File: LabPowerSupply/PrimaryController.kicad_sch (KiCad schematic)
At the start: 19 parts

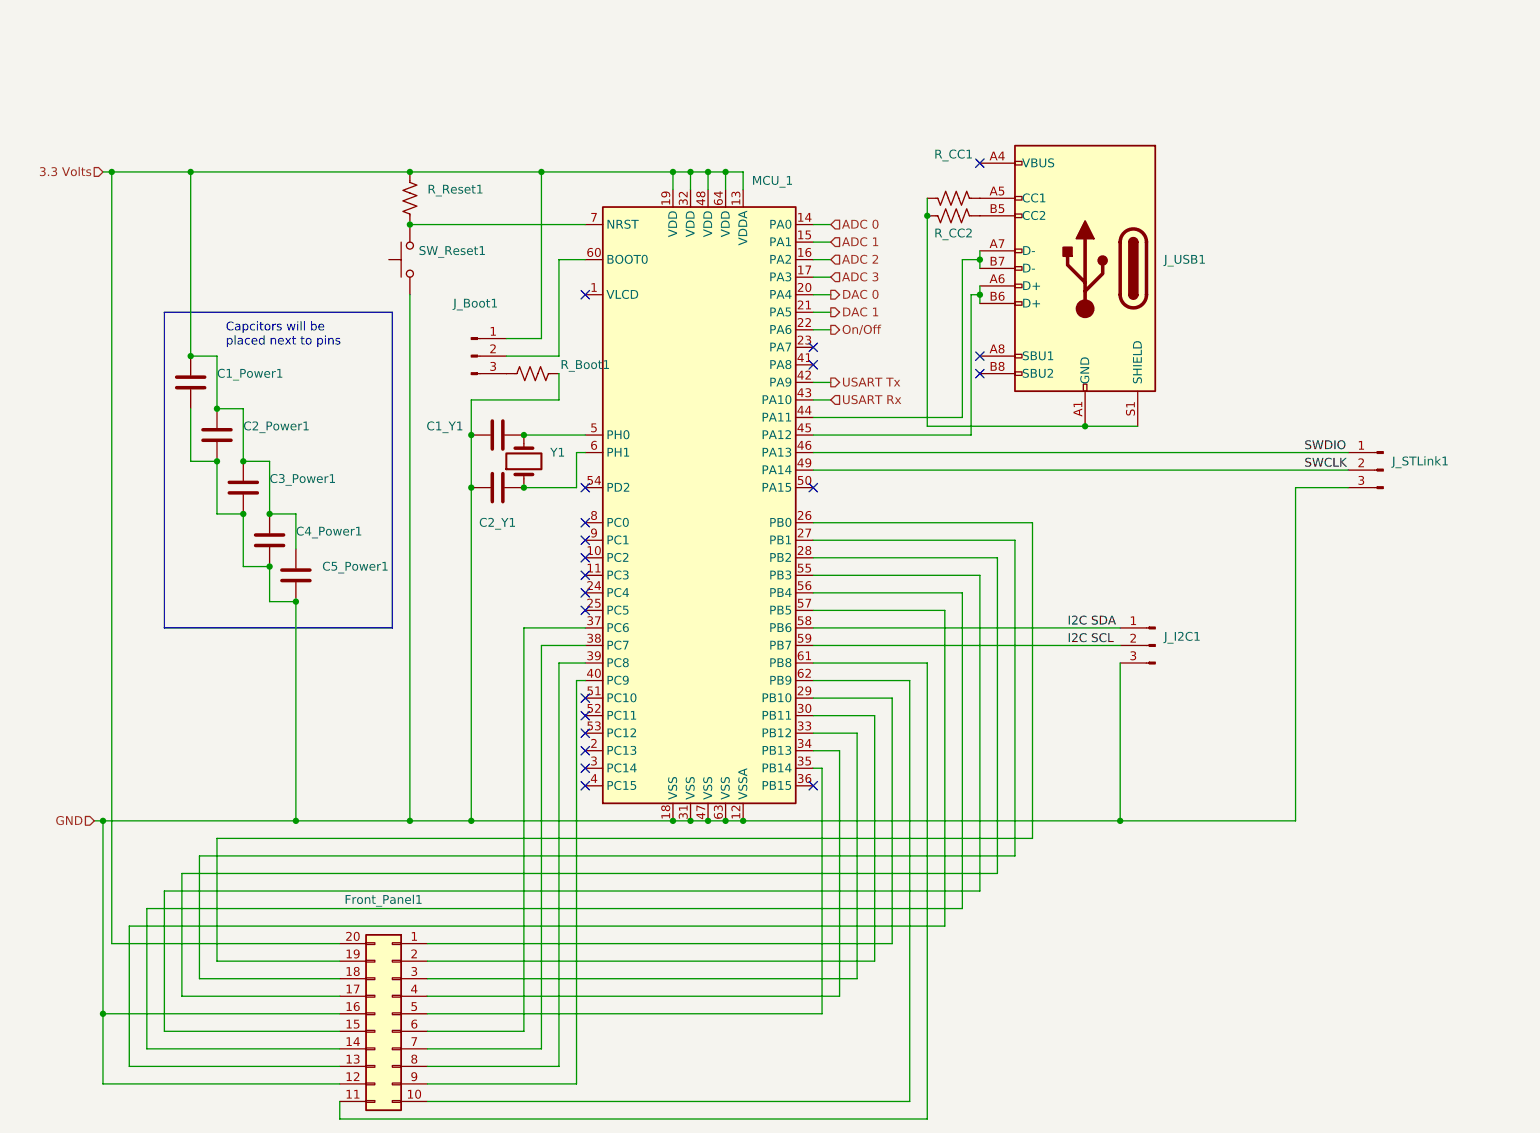
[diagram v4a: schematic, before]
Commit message: Added mcu capacitors, split 5v inductors
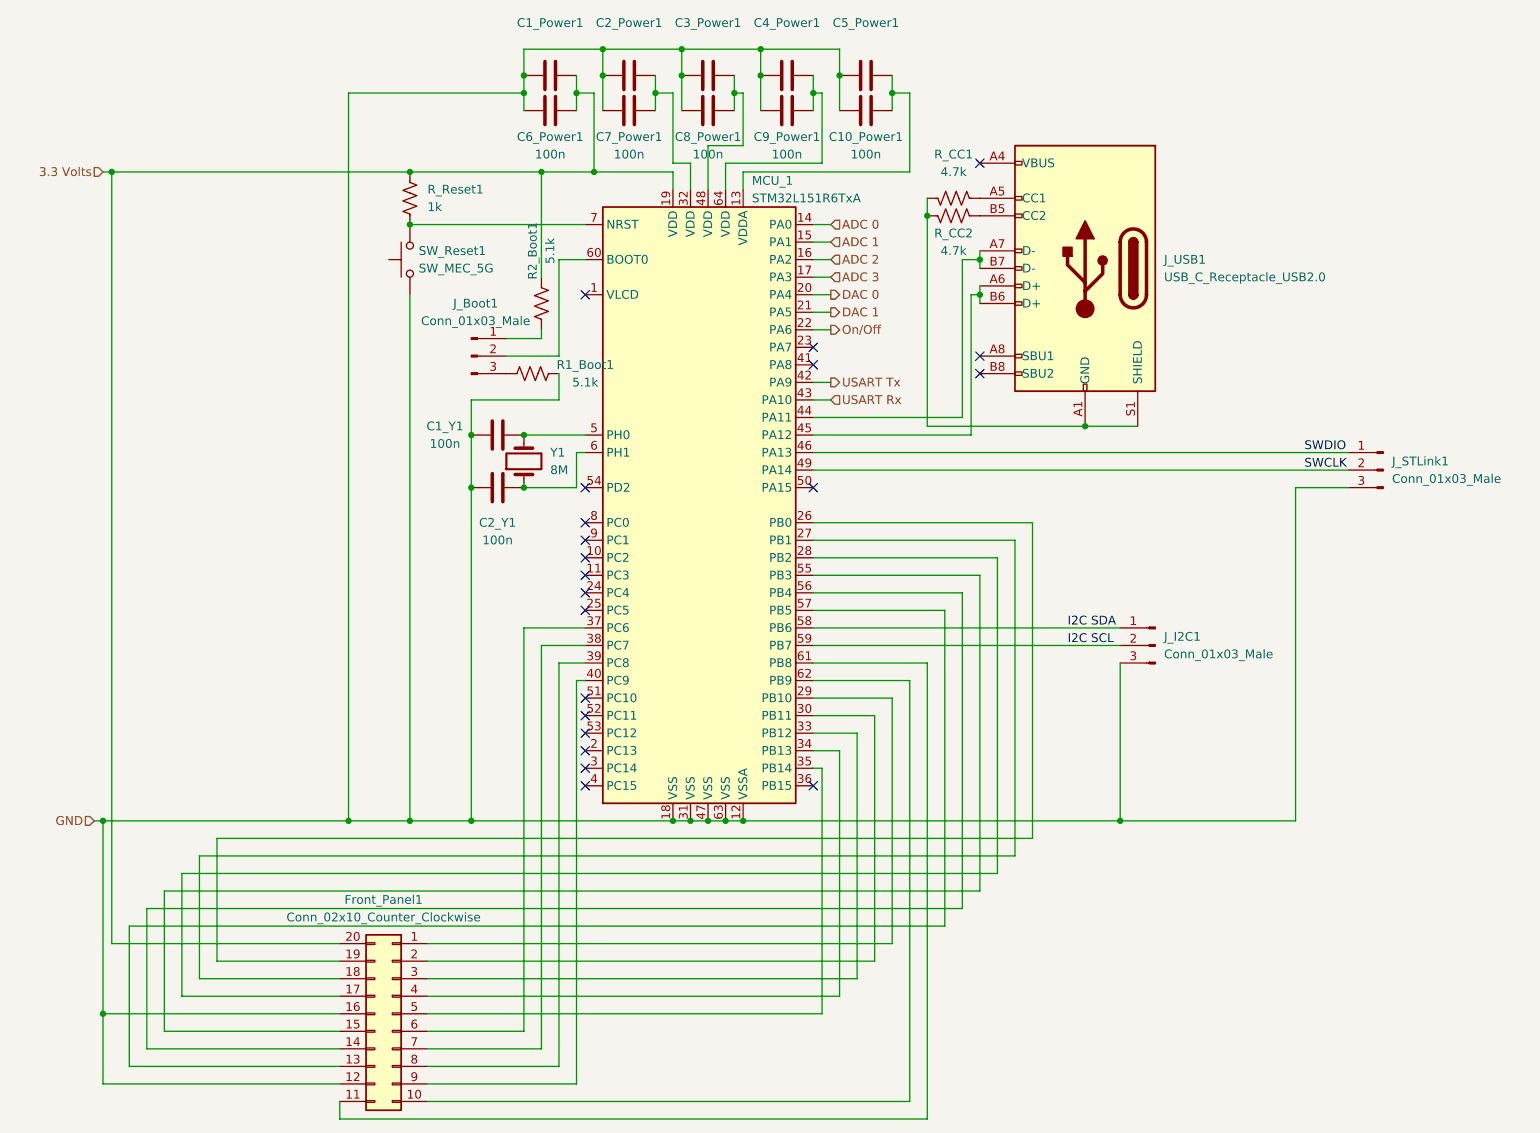
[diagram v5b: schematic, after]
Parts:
- added C10_Power1, C6_Power1, C7_Power1, C8_Power1, C9_Power1: 100n, Capacitor_THT:C_Disc_D5.0mm_W2.5mm_P2.50mm, symbol Device:C
- added R2_Boot1: 5.1k, Resistor_SMD:R_0603_1608Metric, symbol Device:R_US
- C1_Power1, C2_Power1, C3_Power1, C4_Power1, C5_Power1: footprint (none) -> Capacitor_THT:C_Disc_D5.0mm_W2.5mm_P2.50mm
- C1_Y1, C2_Y1: value (none) -> 100n; footprint (none) -> Capacitor_THT:C_Disc_D5.0mm_W2.5mm_P2.50mm
- Front_Panel1: value (none) -> Conn_02x10_Counter_Clockwise; footprint (none) -> Connector_IDC:IDC-Header_2x10_P2.54mm_Vertical
- J_Boot1, J_I2C1, J_STLink1: value (none) -> Conn_01x03_Male; footprint (none) -> Connector_PinHeader_2.54mm:PinHeader_1x03_P2.54mm_Vertical
- J_USB1: value (none) -> USB_C_Receptacle_USB2.0; footprint (none) -> Connector_USB:USB_C_Receptacle_Palconn_UTC16-G
- MCU_1: value (none) -> STM32L151R6TxA; footprint (none) -> Package_QFP:LQFP-64_10x10mm_P0.5mm
- R1_Boot1: renamed from R_Boot1; value (none) -> 5.1k; footprint (none) -> Resistor_SMD:R_0603_1608Metric
- R_CC1, R_CC2: value (none) -> 4.7k; footprint (none) -> Resistor_SMD:R_0603_1608Metric
- R_Reset1: value (none) -> 1k; footprint (none) -> Resistor_SMD:R_0603_1608Metric
- SW_Reset1: value (none) -> SW_MEC_5G; footprint (none) -> Button_Switch_SMD:SW_MEC_5GSH9
- Y1: value (none) -> 8M; footprint (none) -> Crystal:Crystal_HC18-U_Vertical
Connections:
- net 3.3 Volts: now also C1_Power1.2, C6_Power1.2, R2_Boot1.2; no longer C1_Power1.1, C2_Power1.1, C3_Power1.1, C4_Power1.1, C5_Power1.1, J_Boot1.1 (Pin_1), MCU_1.13 (VDDA), MCU_1.32 (VDD), MCU_1.48 (VDD), MCU_1.64 (VDD)
- net GND: now also C1_Power1.1, C2_Power1.1, C3_Power1.1, C4_Power1.1, C5_Power1.1, C10_Power1.1, C6_Power1.1, C7_Power1.1, C8_Power1.1, C9_Power1.1; no longer C1_Power1.2, C2_Power1.2, C3_Power1.2, C4_Power1.2, C5_Power1.2
- new net: C4_Power1.2, C9_Power1.2, MCU_1.64 (VDD)
- new net: C3_Power1.2, C8_Power1.2, MCU_1.48 (VDD)
- new net: C10_Power1.2, C5_Power1.2, MCU_1.13 (VDDA)
- new net: J_Boot1.1 (Pin_1), R2_Boot1.1
- new net: C2_Power1.2, C7_Power1.2, MCU_1.32 (VDD)
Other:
- note removed: "Capcitors will be placed next to pins"
- moved on the sheet: C1_Power1, C2_Power1, C3_Power1, C4_Power1, C5_Power1

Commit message: Added oscillator to mcu2
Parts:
- C1_Power1, C2_Power1, C3_Power1, C4_Power1, C5_Power1: value (none) -> 1u
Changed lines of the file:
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@@
     (in_bom yes) (on_board yes) (fields_autoplaced)
     (property "Reference" "C4_Power1" (id 0) (at 132.08 15.24 90))
-    (property "Value" "" (id 1) (at 132.08 17.78 90))
+    (property "Value" "1u" (id 1) (at 132.08 17.78 90))
     (property "Footprint" "Capacitor_THT:C_Disc_D5.0mm_W2.5mm_P2.50mm" (id 2) (at 135.89 21.8948 0)
       (effects (font (size 1.27 1.27)) hide)
@@
     (in_bom yes) (on_board yes) (fields_autoplaced)
     (property "Reference" "C5_Power1" (id 0) (at 143.51 15.24 90))
-    (property "Value" "" (id 1) (at 143.51 17.78 90))
+    (property "Value" "1u" (id 1) (at 143.51 17.78 90))
     (property "Footprint" "Capacitor_THT:C_Disc_D5.0mm_W2.5mm_P2.50mm" (id 2) (at 147.32 21.8948 0)
       (effects (font (size 1.27 1.27)) hide)
@@
     (in_bom yes) (on_board yes) (fields_autoplaced)
     (property "Reference" "C2_Power1" (id 0) (at 109.22 15.24 90))
-    (property "Value" "" (id 1) (at 109.22 17.78 90))
+    (property "Value" "1u" (id 1) (at 109.22 17.78 90))
     (property "Footprint" "Capacitor_THT:C_Disc_D5.0mm_W2.5mm_P2.50mm" (id 2) (at 113.03 21.8948 0)
       (effects (font (size 1.27 1.27)) hide)
@@
     (in_bom yes) (on_board yes) (fields_autoplaced)
     (property "Reference" "C1_Power1" (id 0) (at 97.79 15.24 90))
-    (property "Value" "" (id 1) (at 97.79 17.78 90))
+    (property "Value" "1u" (id 1) (at 97.79 17.78 90))
     (property "Footprint" "Capacitor_THT:C_Disc_D5.0mm_W2.5mm_P2.50mm" (id 2) (at 101.6 21.8948 0)
       (effects (font (size 1.27 1.27)) hide)
@@
     (in_bom yes) (on_board yes) (fields_autoplaced)
     (property "Reference" "C3_Power1" (id 0) (at 120.65 15.24 90))
-    (property "Value" "" (id 1) (at 120.65 17.78 90))
+    (property "Value" "1u" (id 1) (at 120.65 17.78 90))
     (property "Footprint" "Capacitor_THT:C_Disc_D5.0mm_W2.5mm_P2.50mm" (id 2) (at 124.46 21.8948 0)
       (effects (font (size 1.27 1.27)) hide)

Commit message: Fixed mcu supply
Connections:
- net 3.3 Volts: now also C10_Power1.2, C2_Power1.2, C3_Power1.2, C4_Power1.2, C5_Power1.2, C7_Power1.2, C8_Power1.2, C9_Power1.2, MCU_1.13 (VDDA), MCU_1.32 (VDD), MCU_1.48 (VDD), MCU_1.64 (VDD)
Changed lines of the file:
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@@
   (junction (at 135.89 25.4) (diameter 0) (color 0 0 0 0)
   )
+  (junction (at 118.11 36.83) (diameter 0) (color 0 0 0 0)
+  )
   (junction (at 105.41 19.05) (diameter 0) (color 0 0 0 0)
   )
   (junction (at 115.57 130.81) (diameter 0) (color 0 0 0 0)
   )
+  (junction (at 125.73 36.83) (diameter 0) (color 0 0 0 0)
+  )
   (junction (at 33.02 130.81) (diameter 0) (color 0 0 0 0)
   )
+  (junction (at 120.65 36.83) (diameter 0) (color 0 0 0 0)
+  )
   (junction (at 120.65 130.81) (diameter 0) (color 0 0 0 0)
   )
@@
   (junction (at 147.32 25.4) (diameter 0) (color 0 0 0 0)
   )
+  (junction (at 115.57 36.83) (diameter 0) (color 0 0 0 0)
+  )
   (junction (at 93.98 25.4) (diameter 0) (color 0 0 0 0)
   )
@@
   )
   (junction (at 152.4 43.18) (diameter 0) (color 0 0 0 0)
+  )
+  (junction (at 123.19 36.83) (diameter 0) (color 0 0 0 0)
   )
   (junction (at 93.98 74.93) (diameter 0) (color 0 0 0 0)
@@
     (stroke (width 0) (type default) (color 0 0 0 0))
   )
-  (wire (pts (xy 123.19 35.56) (xy 123.19 39.37))
+  (wire (pts (xy 123.19 35.56) (xy 123.19 36.83))
     (stroke (width 0) (type default) (color 0 0 0 0))
   )
@@
     (stroke (width 0) (type default) (color 0 0 0 0))
   )
+  (wire (pts (xy 123.19 36.83) (xy 125.73 36.83))
+    (stroke (width 0) (type default) (color 0 0 0 0))
+  )
   (wire (pts (xy 93.98 74.93) (xy 102.87 74.93))
     (stroke (width 0) (type default) (color 0 0 0 0))
@@
     (stroke (width 0) (type default) (color 0 0 0 0))
   )
+  (wire (pts (xy 118.11 36.83) (xy 120.65 36.83))
+    (stroke (width 0) (type default) (color 0 0 0 0))
+  )
   (wire (pts (xy 135.89 54.61) (xy 138.43 54.61))
     (stroke (width 0) (type default) (color 0 0 0 0))
   )
-  (wire (pts (xy 120.65 33.02) (xy 120.65 39.37))
+  (wire (pts (xy 120.65 33.02) (xy 120.65 36.83))
     (stroke (width 0) (type default) (color 0 0 0 0))
   )
@@
     (stroke (width 0) (type default) (color 0 0 0 0))
   )
+  (wire (pts (xy 115.57 36.83) (xy 118.11 36.83))
+    (stroke (width 0) (type default) (color 0 0 0 0))
+  )
   (wire (pts (xy 135.89 25.4) (xy 135.89 27.94))
     (stroke (width 0) (type default) (color 0 0 0 0))
@@
     (stroke (width 0) (type default) (color 0 0 0 0))
   )
-  (wire (pts (xy 118.11 35.56) (xy 118.11 39.37))
+  (wire (pts (xy 120.65 36.83) (xy 120.65 39.37))
+    (stroke (width 0) (type default) (color 0 0 0 0))
+  )
+  (wire (pts (xy 118.11 35.56) (xy 118.11 36.83))
     (stroke (width 0) (type default) (color 0 0 0 0))
   )
@@
     (stroke (width 0) (type default) (color 0 0 0 0))
   )
+  (wire (pts (xy 118.11 36.83) (xy 118.11 39.37))
+    (stroke (width 0) (type default) (color 0 0 0 0))
+  )
   (wire (pts (xy 34.29 36.83) (xy 77.47 36.83))
     (stroke (width 0) (type default) (color 0 0 0 0))
@@
     (stroke (width 0) (type default) (color 0 0 0 0))
   )
+  (wire (pts (xy 120.65 36.83) (xy 123.19 36.83))
+    (stroke (width 0) (type default) (color 0 0 0 0))
+  )
   (wire (pts (xy 101.6 25.4) (xy 101.6 27.94))
     (stroke (width 0) (type default) (color 0 0 0 0))
@@
     (stroke (width 0) (type default) (color 0 0 0 0))
   )
+  (wire (pts (xy 123.19 36.83) (xy 123.19 39.37))
+    (stroke (width 0) (type default) (color 0 0 0 0))
+  )
